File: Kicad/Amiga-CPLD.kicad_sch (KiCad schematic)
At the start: 21 parts, among them CN1 CDTV-DIAG, J1 JTAG, J4 LED, SW1 SW_DIP_x04, U1 AZ1117-3.3, U2 XC95144XL-TQ100, X1 50MHz

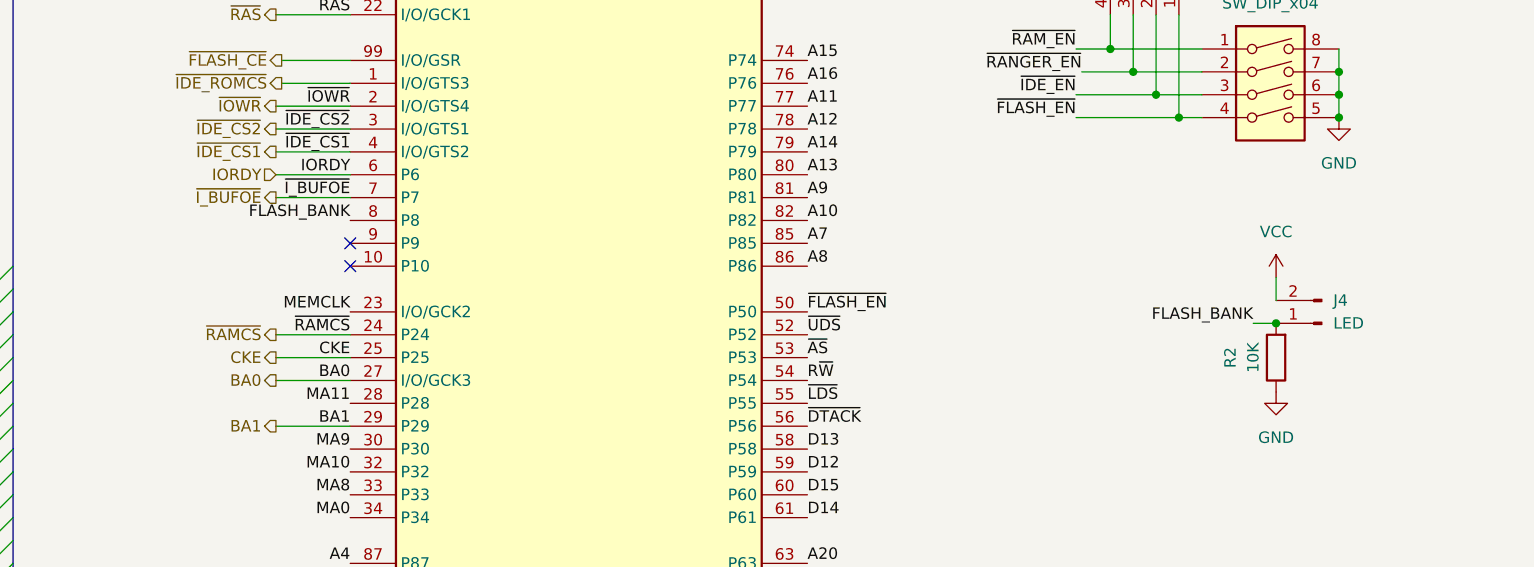
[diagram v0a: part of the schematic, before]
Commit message: PCB: Connect Flash A18 to CPLD
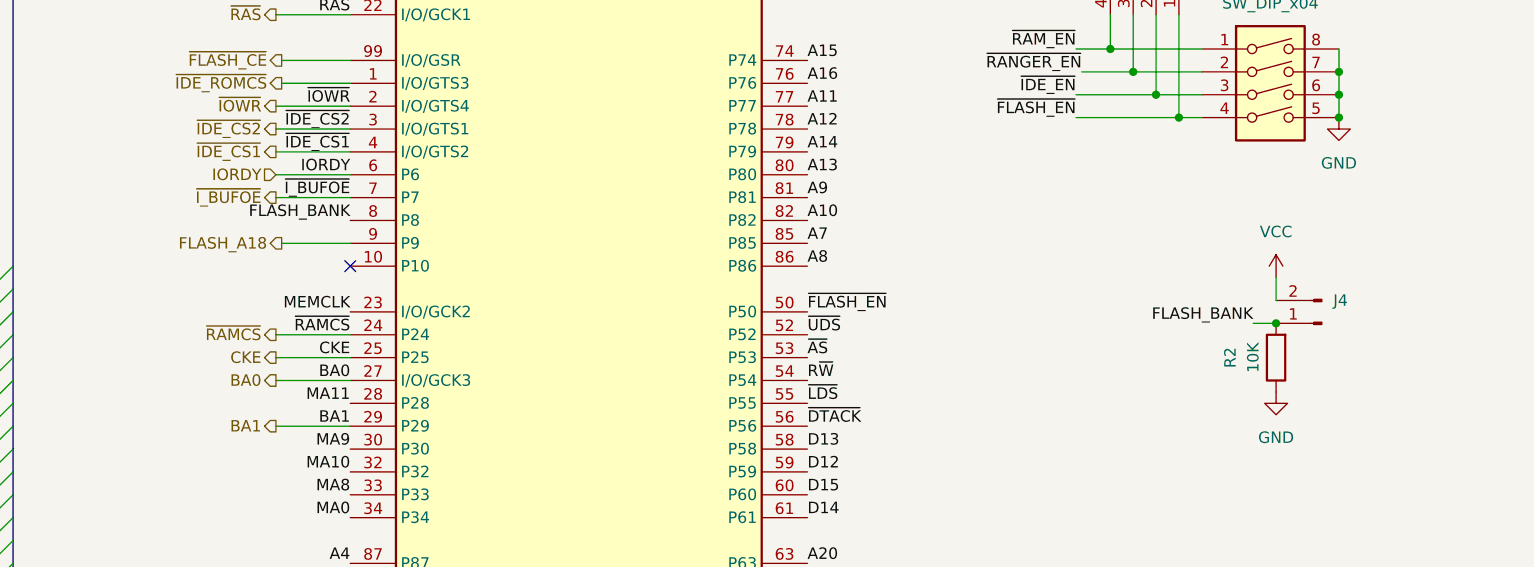
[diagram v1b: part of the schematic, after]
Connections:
- net FLASH_A18: now reaches U2.9 (P9)
- no-connect marks 26 -> 25
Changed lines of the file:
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@@
   (no_connect (at 133.35 39.37))
   (no_connect (at 133.35 41.91))
-  (no_connect (at 133.35 82.55))
   (no_connect (at 133.35 85.09))
   (no_connect (at 40.005 97.79))
@@
     (stroke (width 0) (type default) (color 0 0 0 0))
   )
+  (wire (pts (xy 125.73 82.55) (xy 133.35 82.55))
+    (stroke (width 0) (type default) (color 0 0 0 0))
+  )
   (wire (pts (xy 81.915 57.15) (xy 86.995 57.15))
     (stroke (width 0) (type default) (color 0 0 0 0))
@@
   )
   (hierarchical_label "~{IDE_CS2}" (shape output) (at 125.095 69.85 180)
+    (effects (font (size 1.27 1.27)) (justify right))
+  )
+  (hierarchical_label "FLASH_A18" (shape output) (at 125.73 82.55 180)
     (effects (font (size 1.27 1.27)) (justify right))
   )
@@
     )
     (property "Value" "LED" (id 1) (at 242.57 91.4399 0)
-      (effects (font (size 1.27 1.27)) (justify right))
+      (effects (font (size 1.27 1.27)) (justify right) hide)
     )
     (property "Footprint" "Connector_PinHeader_2.00mm:PinHeader_1x02_P2.00mm_Vertical" (id 2) (at 241.3 91.44 0)

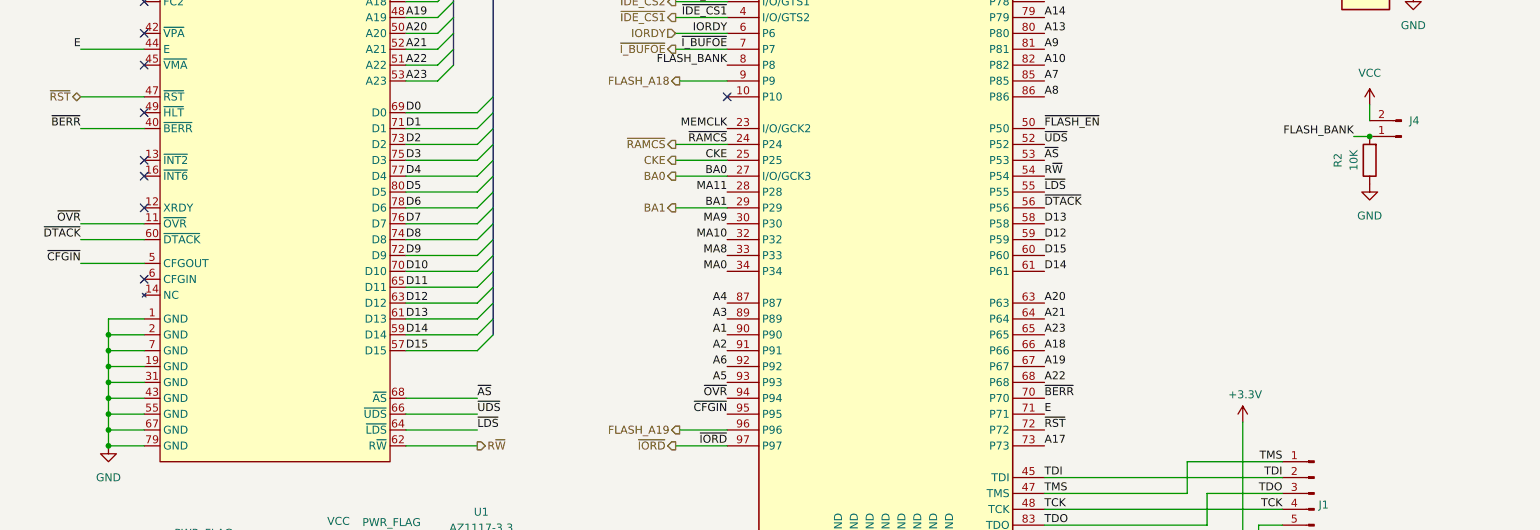
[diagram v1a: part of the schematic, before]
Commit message: PCB: Remove useless cfgin connection
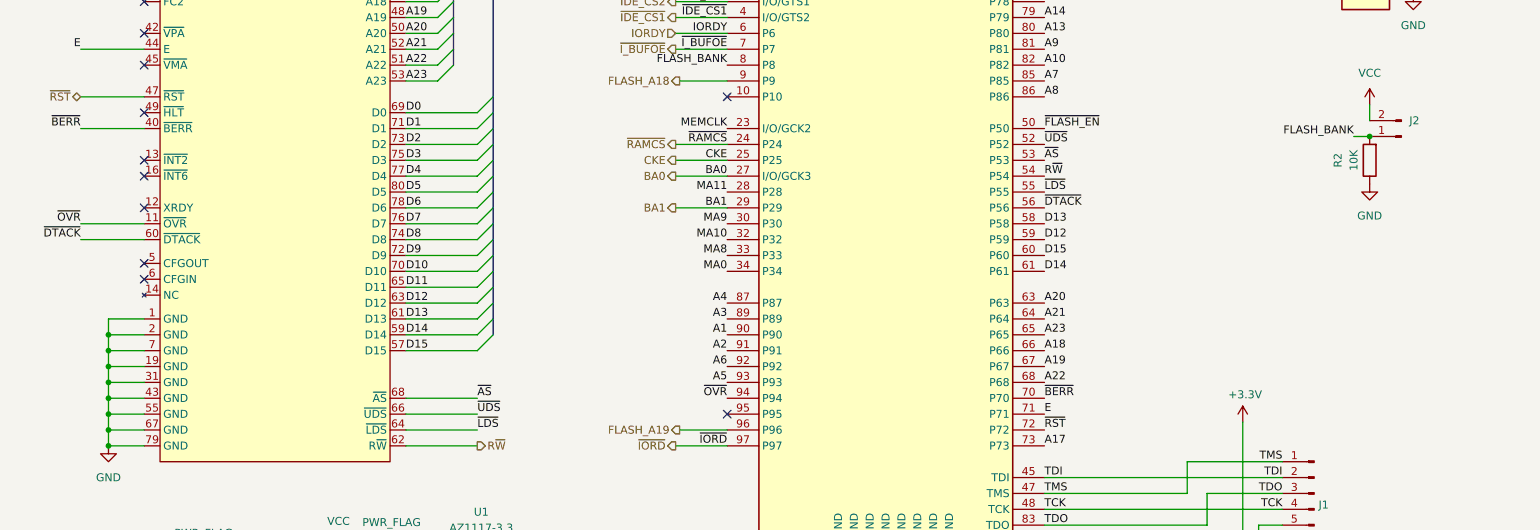
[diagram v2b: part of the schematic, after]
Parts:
- renumbered J4 to J2
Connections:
- net ~{CFGIN}: no longer names the net of U2.95 (P95)
- net ~{CFGIN}: no longer CN1.5 (CFGOUT)
- no-connect marks 25 -> 27
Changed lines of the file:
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@@
   (no_connect (at 40.005 46.99))
   (no_connect (at 40.005 49.53))
+  (no_connect (at 40.005 111.76))
   (no_connect (at 133.35 31.75))
   (no_connect (at 133.35 34.29))
@@
   (no_connect (at 40.005 69.85))
   (no_connect (at 40.005 114.3))
+  (no_connect (at 133.35 135.89))
   (no_connect (at 40.005 95.25))
   (bus_entry (at 86.995 72.39) (size 2.54 -2.54)
@@
     (stroke (width 0) (type default) (color 0 0 0 0))
   )
-  (wire (pts (xy 29.845 111.76) (xy 40.005 111.76))
-    (stroke (width 0) (type default) (color 0 0 0 0))
-  )
   (wire (pts (xy 101.6 158.115) (xy 106.68 158.115))
     (stroke (width 0) (type solid) (color 0 0 0 0))
@@
     (effects (font (size 1.27 1.27)) (justify left bottom))
   )
-  (label "~{CFGIN}" (at 29.845 111.76 180)
-    (effects (font (size 1.27 1.27)) (justify right bottom))
-  )
   (label "MA10" (at 133.35 107.95 180)
     (effects (font (size 1.27 1.27)) (justify right bottom))
@@
   (label "D0" (at 81.915 87.63 0)
     (effects (font (size 1.27 1.27)) (justify left bottom))
-  )
-  (label "~{CFGIN}" (at 133.35 135.89 180)
-    (effects (font (size 1.27 1.27)) (justify right bottom))
   )
   (label "IORDY" (at 133.35 74.93 180)
@@
   (symbol (lib_id "power:VCC") (at 71.12 158.115 0) (unit 1)
     (in_bom yes) (on_board yes) (fields_autoplaced)
-    (property "Reference" "#PWR011" (id 0) (at 71.12 161.925 0)
+    (property "Reference" "#PWR09" (id 0) (at 71.12 161.925 0)
       (effects (font (size 1.27 1.27)) hide)
     )
@@
   (symbol (lib_id "power:+3.3V") (at 38.735 175.895 0) (unit 1)
     (in_bom yes) (on_board yes) (fields_autoplaced)
-    (property "Reference" "#PWR04" (id 0) (at 38.735 179.705 0)
+    (property "Reference" "#PWR02" (id 0) (at 38.735 179.705 0)
       (effects (font (size 1.27 1.27)) hide)
     )
@@
   (symbol (lib_id "power:+3.3V") (at 69.215 180.34 0) (unit 1)
     (in_bom yes) (on_board yes) (fields_autoplaced)
-    (property "Reference" "#PWR010" (id 0) (at 69.215 184.15 0)
+    (property "Reference" "#PWR08" (id 0) (at 69.215 184.15 0)
       (effects (font (size 1.27 1.27)) hide)
     )
@@
   (symbol (lib_id "power:+3.3V") (at 115.57 158.115 0) (unit 1)
     (in_bom yes) (on_board yes) (fields_autoplaced)
-    (property "Reference" "#PWR013" (id 0) (at 115.57 161.925 0)
+    (property "Reference" "#PWR011" (id 0) (at 115.57 161.925 0)
       (effects (font (size 1.27 1.27)) hide)
     )
@@
   (symbol (lib_id "power:GND") (at 122.555 185.42 0) (unit 1)
     (in_bom yes) (on_board yes)
-    (property "Reference" "#PWR014" (id 0) (at 122.555 191.77 0)
+    (property "Reference" "#PWR012" (id 0) (at 122.555 191.77 0)
       (effects (font (size 1.27 1.27)) hide)
     )
@@
   (symbol (lib_id "power:VCC") (at 236.22 86.36 0) (unit 1)
     (in_bom yes) (on_board yes) (fields_autoplaced)
-    (property "Reference" "#PWR08" (id 0) (at 236.22 90.17 0)
+    (property "Reference" "#PWR020" (id 0) (at 236.22 90.17 0)
       (effects (font (size 1.27 1.27)) hide)
     )
@@
   (symbol (lib_id "power:GND") (at 218.44 158.75 0) (unit 1)
     (in_bom yes) (on_board yes)
-    (property "Reference" "#PWR018" (id 0) (at 218.44 165.1 0)
+    (property "Reference" "#PWR019" (id 0) (at 218.44 165.1 0)
       (effects (font (size 1.27 1.27)) hide)
     )
@@
   (symbol (lib_id "power:+3V3") (at 217.805 46.99 0) (unit 1)
     (in_bom yes) (on_board yes) (fields_autoplaced)
-    (property "Reference" "#PWR0102" (id 0) (at 217.805 50.8 0)
+    (property "Reference" "#PWR018" (id 0) (at 217.805 50.8 0)
       (effects (font (size 1.27 1.27)) hide)
     )
@@
   (symbol (lib_id "power:GND") (at 34.29 140.97 0) (unit 1)
     (in_bom yes) (on_board yes) (fields_autoplaced)
-    (property "Reference" "#PWR03" (id 0) (at 34.29 147.32 0)
+    (property "Reference" "#PWR01" (id 0) (at 34.29 147.32 0)
       (effects (font (size 1.27 1.27)) hide)
     )
@@
   (symbol (lib_id "power:GND") (at 57.785 185.42 0) (unit 1)
     (in_bom yes) (on_board yes) (fields_autoplaced)
-    (property "Reference" "#PWR09" (id 0) (at 57.785 191.77 0)
+    (property "Reference" "#PWR07" (id 0) (at 57.785 191.77 0)
       (effects (font (size 1.27 1.27)) hide)
     )
@@
   (symbol (lib_id "power:VCC") (at 57.785 180.34 0) (unit 1)
     (in_bom yes) (on_board yes) (fields_autoplaced)
-    (property "Reference" "#PWR0103" (id 0) (at 57.785 184.15 0)
+    (property "Reference" "#PWR06" (id 0) (at 57.785 184.15 0)
       (effects (font (size 1.27 1.27)) hide)
     )
@@
   (symbol (lib_id "power:GND") (at 243.205 68.58 0) (unit 1)
     (in_bom yes) (on_board yes) (fields_autoplaced)
-    (property "Reference" "#PWR020" (id 0) (at 243.205 74.93 0)
+    (property "Reference" "#PWR022" (id 0) (at 243.205 74.93 0)
       (effects (font (size 1.27 1.27)) hide)
     )
@@
   (symbol (lib_id "power:GND") (at 93.98 165.735 0) (unit 1)
     (in_bom yes) (on_board yes)
-    (property "Reference" "#PWR012" (id 0) (at 93.98 172.085 0)
+    (property "Reference" "#PWR010" (id 0) (at 93.98 172.085 0)
       (effects (font (size 1.27 1.27)) hide)
     )
@@
   (symbol (lib_id "power:GND") (at 146.685 187.325 0) (unit 1)
     (in_bom yes) (on_board yes)
-    (property "Reference" "#PWR02" (id 0) (at 146.685 193.675 0)
+    (property "Reference" "#PWR014" (id 0) (at 146.685 193.675 0)
       (effects (font (size 1.27 1.27)) hide)
     )
@@
   (symbol (lib_id "power:GND") (at 38.735 188.595 0) (unit 1)
     (in_bom yes) (on_board yes)
-    (property "Reference" "#PWR05" (id 0) (at 38.735 194.945 0)
+    (property "Reference" "#PWR03" (id 0) (at 38.735 194.945 0)
       (effects (font (size 1.27 1.27)) hide)
     )
@@
   (symbol (lib_id "power:VCC") (at 40.005 19.685 0) (unit 1)
     (in_bom yes) (on_board yes) (fields_autoplaced)
-    (property "Reference" "#PWR06" (id 0) (at 40.005 23.495 0)
+    (property "Reference" "#PWR04" (id 0) (at 40.005 23.495 0)
       (effects (font (size 1.27 1.27)) hide)
     )
@@
   (symbol (lib_id "power:GND") (at 236.22 99.06 0) (unit 1)
     (in_bom yes) (on_board yes) (fields_autoplaced)
-    (property "Reference" "#PWR019" (id 0) (at 236.22 105.41 0)
+    (property "Reference" "#PWR021" (id 0) (at 236.22 105.41 0)
       (effects (font (size 1.27 1.27)) hide)
     )
@@
   (symbol (lib_id "power:+3.3V") (at 146.685 172.085 0) (unit 1)
     (in_bom yes) (on_board yes)
-    (property "Reference" "#PWR01" (id 0) (at 146.685 175.895 0)
+    (property "Reference" "#PWR013" (id 0) (at 146.685 175.895 0)
       (effects (font (size 1.27 1.27)) hide)
     )
@@
   (symbol (lib_id "Connector:Conn_01x02_Male") (at 241.3 91.44 180) (unit 1)
     (in_bom yes) (on_board yes) (fields_autoplaced)
-    (property "Reference" "J4" (id 0) (at 242.57 88.8999 0)
+    (property "Reference" "J2" (id 0) (at 242.57 88.8999 0)
       (effects (font (size 1.27 1.27)) (justify right))
     )
@@
   (symbol (lib_id "power:GND") (at 49.53 160.02 0) (unit 1)
     (in_bom yes) (on_board yes)
-    (property "Reference" "#PWR07" (id 0) (at 49.53 166.37 0)
-      (effects (font (size 1.27 1.27)) hide)
-    )
+    (property "Reference" "#PWR05" (id 0) (at 49.53 166.37 0)
+      (effects (font (size 1.27 1.27)) hide)
+    )
